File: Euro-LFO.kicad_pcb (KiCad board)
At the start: 2 copper layers, 65.1 x 128.5 mm, 40 parts, among them J1 2×5 2.54 mm shrouded IDC box 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, J3 Conn_01x07_Socket, J4 Conn_01x07_Pin, J5 Conn_01x07_Socket, J6 Conn_01x07_Pin, Q1 MMBT3904, U1 TL074CDR

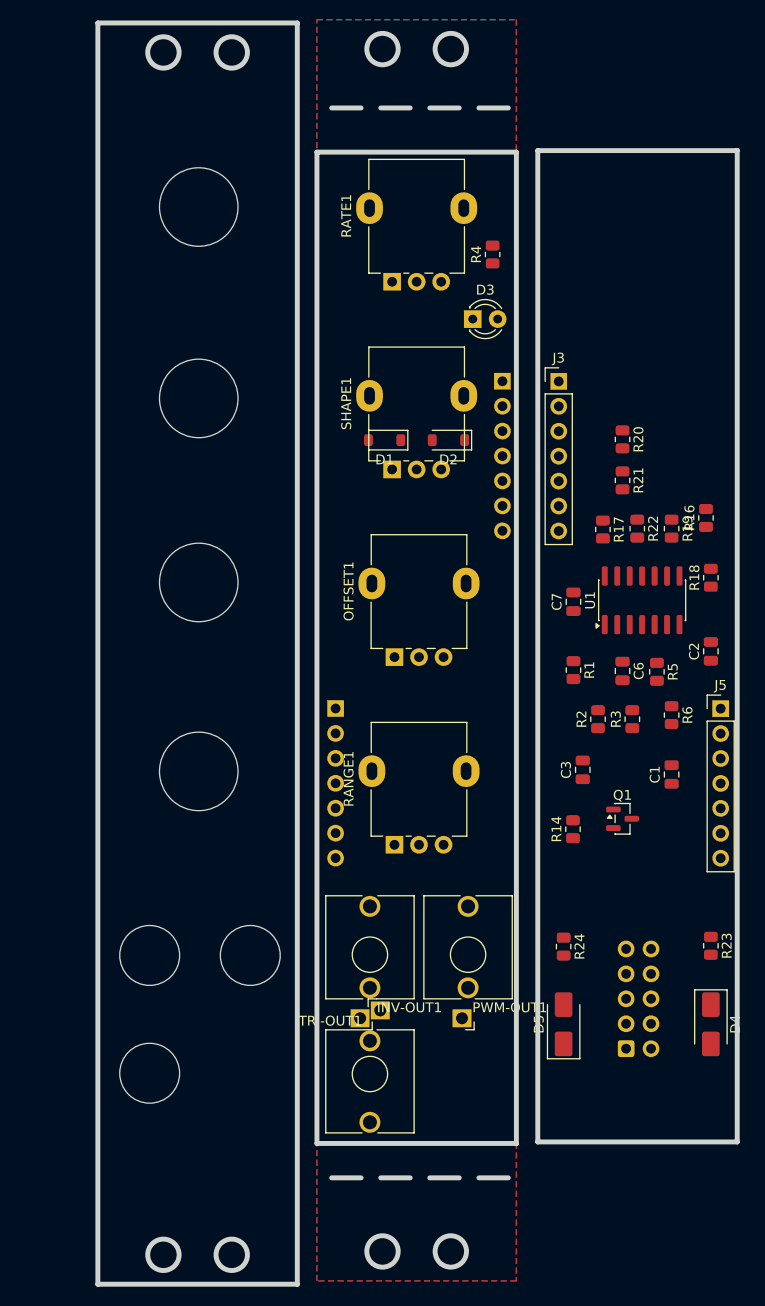
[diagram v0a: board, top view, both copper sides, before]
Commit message: added mousebites
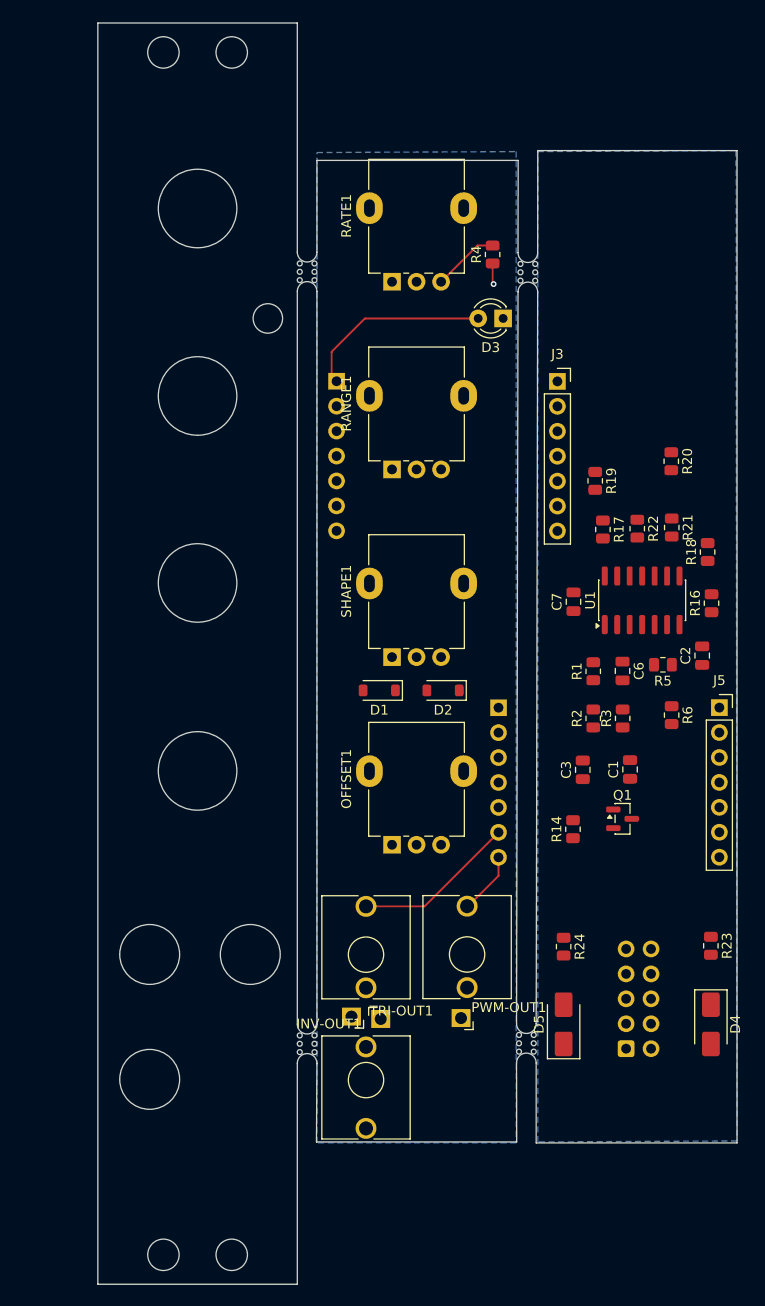
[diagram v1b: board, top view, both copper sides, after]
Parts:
- added REF**: MouseBite-Slot_2.0x2.0mm_outset_D0.5mm_P0.85mm_3h, Panelization:MouseBite-Slot_2.0x2.0mm_outset_D0.5mm_P0.85mm_3h, F.Cu at (101.0, 45.4)
- added REF**: MouseBite-Slot_2.0x2.0mm_outset_D0.5mm_P0.85mm_3h, Panelization:MouseBite-Slot_2.0x2.0mm_outset_D0.5mm_P0.85mm_3h, F.Cu at (101.0, 124.0)
- added REF**: MouseBite-Slot_2.0x2.0mm_outset_D0.5mm_P0.85mm_3h, Panelization:MouseBite-Slot_2.0x2.0mm_outset_D0.5mm_P0.85mm_3h, F.Cu at (123.5, 45.4)
- added REF**: MouseBite-Slot_2.0x2.0mm_outset_D0.5mm_P0.85mm_3h, Panelization:MouseBite-Slot_2.0x2.0mm_outset_D0.5mm_P0.85mm_3h, F.Cu at (123.3, 124.0)
- J3, J5: footprint Connector_PinHeader_2.54mm:PinHeader_1x07_P2.54mm_Vertical -> Connector_PinSocket_2.54mm:PinSocket_1x07_P2.54mm_Vertical
- moved RANGE1 38.2 mm to (108.7, 65.5)
- moved D1 25.5 mm to (107.3, 88.0)
- moved D2 25.5 mm to (113.8, 88.0)
- moved OFFSET1 19.1 mm to (108.7, 103.7)
- moved SHAPE1 19.1 mm to (108.7, 84.6)
- moved J4 16.9 mm to (103.0, 56.5)
- moved J6 16.6 mm to (119.5, 89.8)
- moved R19 9.18 mm to (129.3, 66.7)
- moved R16 8.70 mm to (141.2, 79.1)
- moved R21 6.94 mm to (137.2, 71.4)
- moved R20 5.44 mm to (137.1, 64.7)
- moved C1 4.27 mm to (132.9, 96.0)
- moved D3 3.10 mm to (120.0, 50.1), turned to 180 degrees
- moved R18 2.64 mm to (140.8, 73.9)
- moved R1 2.02 mm to (129.2, 86.0), turned to 90 degrees
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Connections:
- INV-OUT1 pad T: /INV-OUT-A -> /INV_O
- J3 pad 3: unconnected-(J3-Pin_3-Pad3) -> GND
- J3 pad 4: unconnected-(J3-Pin_4-Pad4) -> GND
- J3 pad 5: /PWM_I -> /RNG_2_I
- J3 pad 6: /TRI_I -> /RNG_3_I
- J3 pad 7: GND -> /SHP_I
- J4 pad 2: unconnected-(J4-Pin_2-Pad2) -> /INV_O
- J4 pad 3: unconnected-(J4-Pin_3-Pad3) -> /GND_O
- J4 pad 4: unconnected-(J4-Pin_4-Pad4) -> /GND_O
- J4 pad 5: /PWM_O -> /RNG_2_O
- J4 pad 6: /TRI_O -> /RNG_3_O
- J4 pad 7: /GND_O -> /SHP_O
- J5 pad 5: /RNG_3_I -> -12V
- J5 pad 6: /RNG_2_I -> /TRI_I
- J5 pad 7: unconnected-(J5-Pin_7-Pad7) -> /PWM_I
- J6 pad 5: /RNG_3_O -> /-12_O
- J6 pad 6: /RNG_2_O -> /TRI_O
- J6 pad 7: unconnected-(J6-Pin_7-Pad7) -> /PWM_O
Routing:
- net /LED_O: track 0.00 -> 19.3 mm
- net /TRI_O: track 0.00 -> 16.2 mm
- net Net-(R4-Pad2): track 0.00 -> 6.77 mm
- net /PWM_O: track 0.00 -> 6.28 mm
- net /GND_O: track 0.00 -> 2.14 mm, vias 0 -> 1
- added copper zone on B.Cu, net /GND_O
- added copper zone on B.Cu, net GND
- removed copper zone on B.Cu, net (none)
- removed copper zone on F.Cu, net (none)
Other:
- outline, holes or cut-outs redrawn
- board text added: "LED"
- board text added: "OFFSET"
- board text added: "RANGE"
- board text added: "RATE"
- board text added: "SHAPE"

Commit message: V1 complete
Needs review!
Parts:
- moved R6 1.71 mm to (135.5, 91.0), turned to 90 degrees
- moved INV-OUT1 1.50 mm to (106.0, 122.7)
- moved R14 1.42 mm to (128.5, 102.1)
- moved Q1 0.87 mm to (133.0, 101.1)
- turned C1 to 180 degrees
- turned R17 to 90 degrees
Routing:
- net /INV_O: track 0.00 -> 77.3 mm
- net -12V: track 0.00 -> 64.7 mm, vias 0 -> 4
- net Net-(D1-K): track 0.00 -> 56.4 mm
- net +12V: track 0.00 -> 53.4 mm, vias 0 -> 6
- net /LED_I: track 0.00 -> 48.2 mm
- net /U1A_O: track 0.00 -> 47.9 mm, vias 0 -> 2
- net /RNG_3_I: track 0.00 -> 47.5 mm, vias 0 -> 4
- net /TRI_I: track 0.00 -> 40.9 mm, vias 0 -> 1
- net Net-(U1C--): track 0.00 -> 26.4 mm
- net /SHP_I: track 0.00 -> 25.3 mm
- net Net-(R17-Pad2): track 0.00 -> 24.5 mm, vias 0 -> 2
- net /U1A_I: track 0.00 -> 23.4 mm, vias 0 -> 4
- net /PWM_I: track 0.00 -> 23.1 mm
- net /OFF_I: track 0.00 -> 18.1 mm
- net /+12_O: track 0.00 -> 17.3 mm
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- added copper zone on F.Cu, net (none)
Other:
- outline, holes or cut-outs redrawn
- board text added: "INV"
- board text added: "SQR"
- board text added: "TRI"

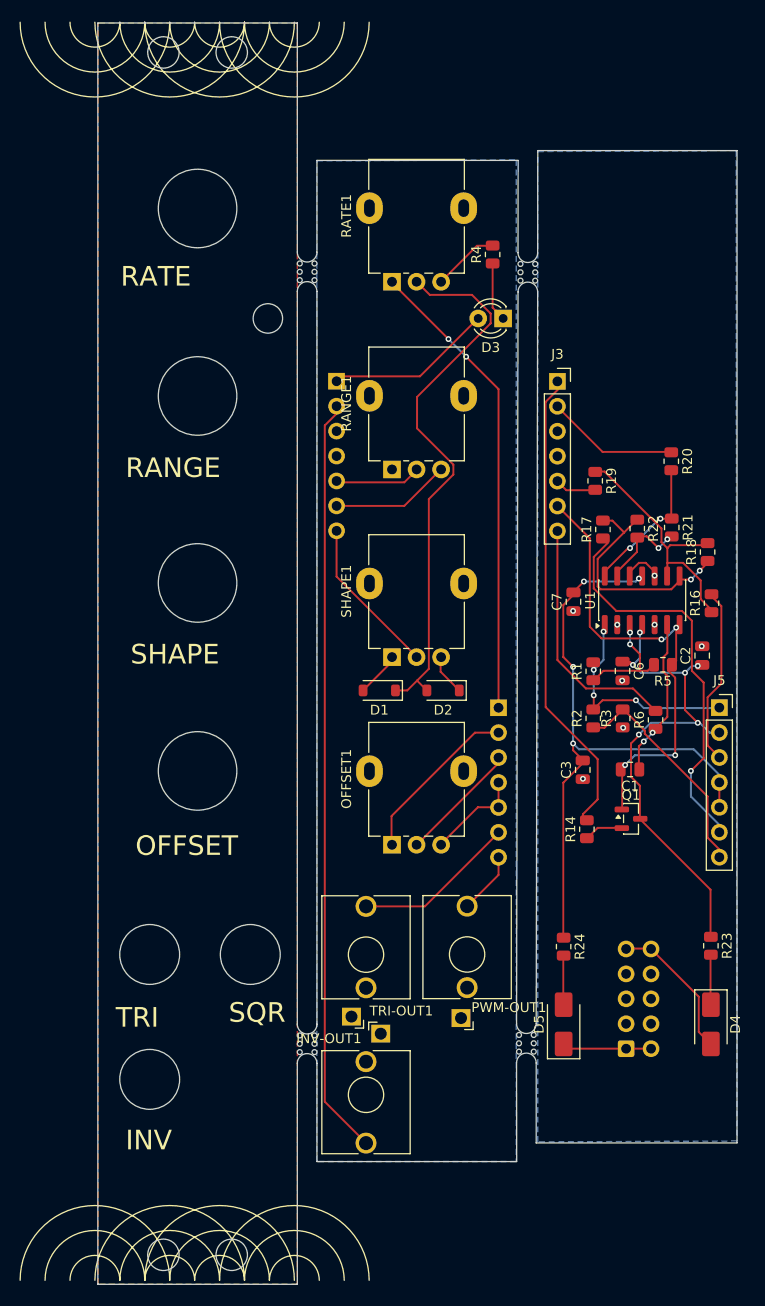
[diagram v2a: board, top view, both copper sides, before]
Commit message: separated front panel
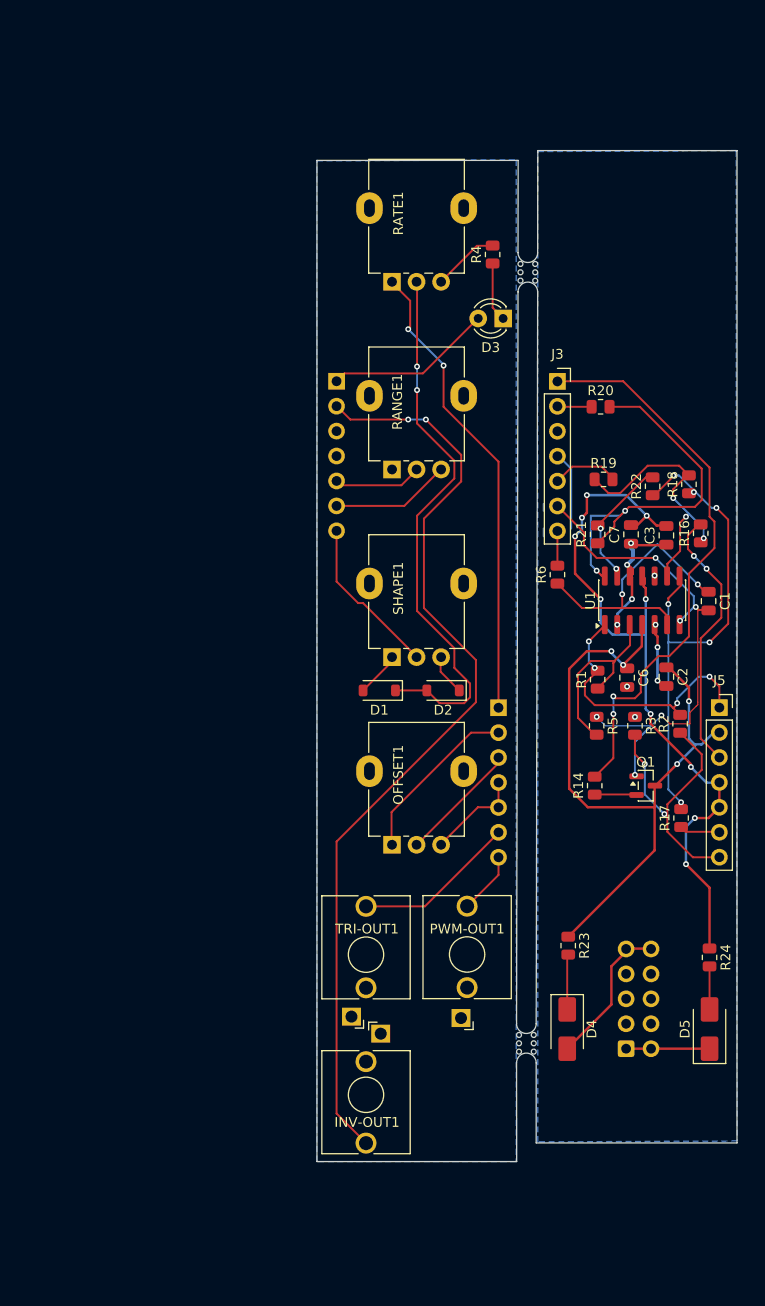
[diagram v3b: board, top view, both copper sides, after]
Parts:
- removed the REF** at (101.0, 45.4)
- removed the REF** at (101.0, 124.0)
- C3: value 00 nF 50 V X7R -> 100 nF 50 V X7R
- U1: value TL074CDR -> LM324DT
- moved R17 30.5 mm to (138.1, 101.0)
- moved C3 25.4 mm to (136.6, 72.2)
- moved C1 18.9 mm to (140.9, 78.9), turned to -90 degrees
- moved R6 17.9 mm to (125.5, 76.2)
- moved R24 14.9 mm to (141.0, 115.2)
- moved D5 14.9 mm to (141.0, 122.5)
- moved D4 14.6 mm to (126.5, 122.5)
- moved R23 14.5 mm to (126.6, 114.0)
- moved R5 9.17 mm to (129.5, 91.6), turned to -90 degrees
- moved R20 9.09 mm to (129.9, 59.1), turned to 0 degrees
- moved C7 9.03 mm to (133.0, 72.1)
- moved R2 8.87 mm to (138.0, 91.4)
- moved R21 7.58 mm to (129.6, 72.1), turned to 90 degrees
- moved R16 7.20 mm to (140.1, 72.0)
- moved R18 7.16 mm to (138.9, 67.0)
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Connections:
- net Net-(D4-A) renamed /PWR_+_IN
- net Net-(D5-K) renamed /PWR_-_IN
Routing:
- net /TRI_I: track 40.9 -> 4.11 mm, vias 1 -> 0
- net Net-(R17-Pad2): track 24.5 -> 53.7 mm, vias 2 -> 6
- net GND: track 4.62 -> 30.5 mm, vias 8 -> 10
- net Net-(R20-Pad2): track 14.5 -> 38.5 mm
- net /SHP_I: track 25.3 -> 3.50 mm
- net /INV_O: track 77.3 -> 95.8 mm, vias 0 -> 2
- net +12V: track 53.4 -> 71.5 mm, vias 6 -> 4
- net Net-(U1B--): track 16.2 -> 28.8 mm
- net -12V: track 64.7 -> 76.3 mm, vias 4 -> 10
- net /INV_I: track 13.5 -> 3.50 mm
- net /LED_I: track 48.2 -> 58.1 mm, vias 0 -> 2
- net /OFF_I: track 18.1 -> 27.2 mm, vias 0 -> 2
- net Net-(U1A-+): track 12.0 -> 19.2 mm, vias 2 -> 0
- net /PWM_I: track 23.1 -> 28.2 mm, vias 0 -> 2
- net /U1A_I: track 23.4 -> 28.2 mm
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- removed copper zone on F.Cu, net (none)
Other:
- board size 65.1 x 128.5 mm -> 42.8 x 103 mm
- board text added: "LFO"
- board text added: "SUPER-FREQ"
- board text removed: "INV"
- board text removed: "LED"
- board text removed: "OFFSET"
- board text removed: "RANGE"
- board text removed: "RATE"
- board text removed: "SHAPE"
- board text removed: "SQR"
- board text removed: "TRI"

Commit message: review and update
Reviewed ad updated board dimensions and outlines. Checked position of jacks and pots.
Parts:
- moved D3 1.80 mm to (118.7, 48.8), turned to -90 degrees
- moved J5 1.10 mm to (140.9, 89.8)
- moved R14 1.10 mm to (128.2, 97.7)
- moved C1 1.10 mm to (139.8, 78.9)
- moved C2 1.10 mm to (135.5, 86.6)
- moved C3 1.10 mm to (135.5, 72.2)
- moved C6 1.10 mm to (131.5, 86.7)
- moved C7 1.10 mm to (131.9, 72.1)
- moved D4 1.10 mm to (125.4, 122.5)
- moved D5 1.10 mm to (139.9, 122.5)
- moved J1 1.10 mm to (131.4, 124.5)
- moved J3 1.10 mm to (124.4, 56.5)
- moved Q1 1.10 mm to (133.4, 97.7)
- moved R1 1.10 mm to (128.5, 86.9)
- moved R16 1.10 mm to (139.0, 72.0)
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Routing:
- net /GND_O: track 6.09 -> 4.41 mm
- net GND: track 30.5 -> 29.0 mm
- net /LED_O: track 17.1 -> 17.8 mm
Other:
- board size 42.8 x 103 mm -> 40.8 x 103 mm
- board text added: "-12V"

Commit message: update
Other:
- board text added: "V1.0"
